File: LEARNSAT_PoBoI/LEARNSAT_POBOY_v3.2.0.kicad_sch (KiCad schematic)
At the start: 0 parts

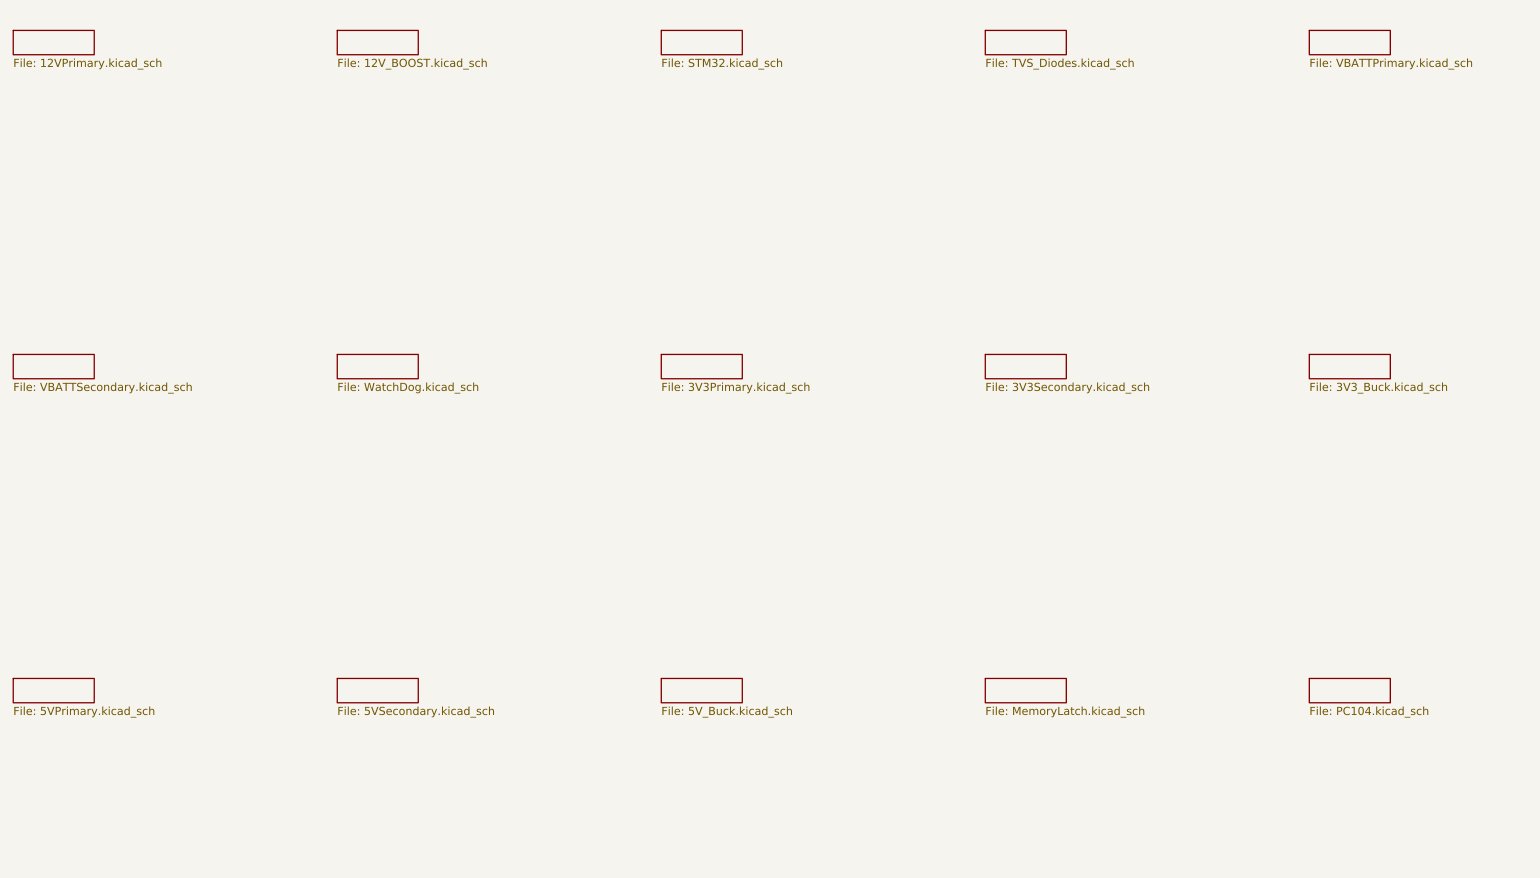
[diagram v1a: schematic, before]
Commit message: Edited 12V Rail schematics
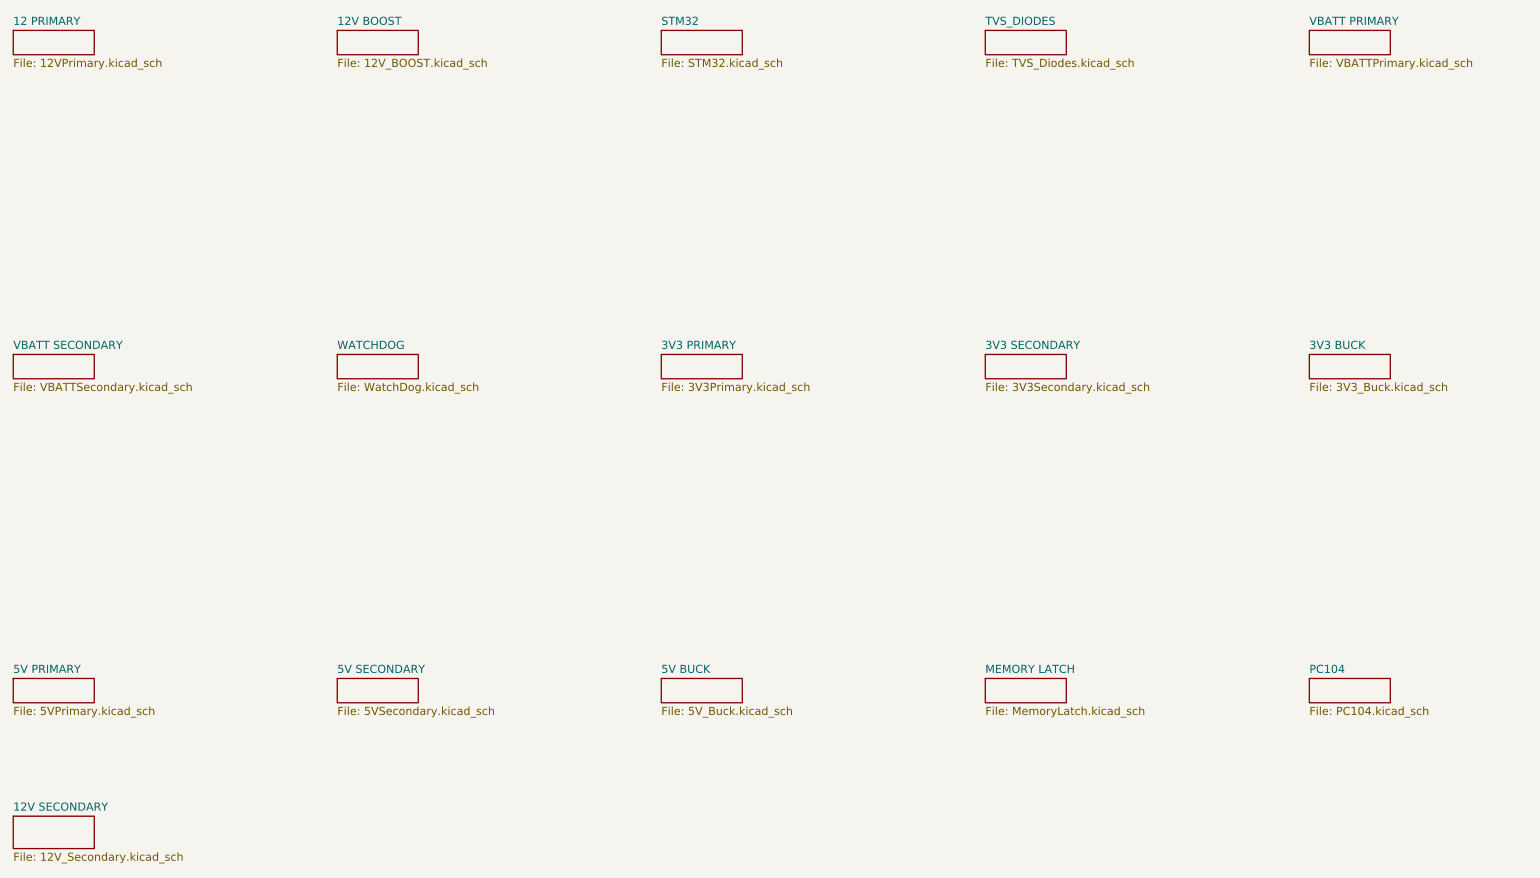
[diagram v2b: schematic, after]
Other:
- sheet  renamed 5V PRIMARY
- added sheet 12 PRIMARY (12VPrimary.kicad_sch)
- added sheet 12V BOOST (12V_BOOST.kicad_sch)
- added sheet 12V SECONDARY (12V_Secondary.kicad_sch)
- added sheet 3V3 BUCK (3V3_Buck.kicad_sch)
- added sheet 3V3 PRIMARY (3V3Primary.kicad_sch)
- added sheet 3V3 SECONDARY (3V3Secondary.kicad_sch)
- added sheet 5V BUCK (5V_Buck.kicad_sch)
- added sheet 5V SECONDARY (5VSecondary.kicad_sch)
- added sheet MEMORY LATCH (MemoryLatch.kicad_sch)
- added sheet PC104 (PC104.kicad_sch)
- added sheet STM32 (STM32.kicad_sch)
- added sheet TVS_DIODES (TVS_Diodes.kicad_sch)
- added sheet VBATT PRIMARY (VBATTPrimary.kicad_sch)
- added sheet VBATT SECONDARY (VBATTSecondary.kicad_sch)
- added sheet WATCHDOG (WatchDog.kicad_sch)
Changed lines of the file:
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@@
 			(color 0 0 0 0)
 		)
-		(property "Sheetname" ""
+		(property "Sheetname" "12V BOOST"
 			(at 76.2 24.6884 0)
 			(show_name no)
@@
 			(color 0 0 0 0)
 		)
-		(property "Sheetname" ""
+		(property "Sheetname" "3V3 BUCK"
 			(at 228.6 75.4884 0)
 			(show_name no)
@@
 			(color 0 0 0 0)
 		)
-		(property "Sheetname" ""
+		(property "Sheetname" "12 PRIMARY"
 			(at 25.4 24.6884 0)
 			(show_name no)
@@
 			(color 0 0 0 0)
 		)
-		(property "Sheetname" ""
+		(property "Sheetname" "WATCHDOG"
 			(at 76.2 75.4884 0)
 			(show_name no)
@@
 			(color 0 0 0 0)
 		)
-		(property "Sheetname" ""
+		(property "Sheetname" "VBATT PRIMARY"
 			(at 228.6 24.6884 0)
 			(show_name no)
@@
 			(color 0 0 0 0)
 		)
-		(property "Sheetname" ""
+		(property "Sheetname" "VBATT SECONDARY"
 			(at 25.4 75.4884 0)
 			(show_name no)
@@
 			(color 0 0 0 0)
 		)
-		(property "Sheetname" ""
+		(property "Sheetname" "5V SECONDARY"
 			(at 76.2 126.2884 0)
 			(show_name no)
@@
 			(color 0 0 0 0)
 		)
-		(property "Sheetname" ""
+		(property "Sheetname" "TVS_DIODES"
 			(at 177.8 24.6884 0)
 			(show_name no)
@@
 			(color 0 0 0 0)
 		)
-		(property "Sheetname" ""
+		(property "Sheetname" "STM32"
 			(at 127 24.6884 0)
 			(show_name no)
@@
 			(color 0 0 0 0)
 		)
-		(property "Sheetname" ""
+		(property "Sheetname" "3V3 SECONDARY"
 			(at 177.8 75.4884 0)
 			(show_name no)
@@
 			(color 0 0 0 0)
 		)
-		(property "Sheetname" ""
+		(property "Sheetname" "MEMORY LATCH"
 			(at 177.8 126.2884 0)
 			(show_name no)
@@
 			(color 0 0 0 0)
 		)
-		(property "Sheetname" ""
+		(property "Sheetname" "3V3 PRIMARY"
 			(at 127 75.4884 0)
 			(show_name no)
@@
 	)
 	(sheet
+		(at 25.4 148.59)
+		(size 12.7 5.08)
+		(exclude_from_sim no)
+		(in_bom yes)
+		(on_board yes)
+		(dnp no)
+		(fields_autoplaced yes)
+		(stroke
+			(width 0.1524)
+			(type solid)
+		)
+		(fill
+			(color 0 0 0 0)
+		)
+		(property "Sheetname" "12V SECONDARY"
+			(at 25.4 147.8784 0)
+			(show_name no)
+			(do_not_autoplace no)
+			(effects
+				(font
+					(size 1.27 1.27)
+				)
+				(justify left bottom)
+			)
+		)
+		(property "Sheetfile" "12V_Secondary.kicad_sch"
+			(at 25.4 154.2546 0)
+			(show_name no)
+			(do_not_autoplace no)
+			(effects
+				(font
+					(size 1.27 1.27)
+				)
+				(justify left top)
+			)
+		)
+		(instances
+			(project "LEARNSAT_POBOY_v3.2.0"
+				(path "/31302da5-a970-4b2b-aa05-afcd06cb9d09"
+					(page "1")
+				)
+			)
+		)
+	)
+	(sheet
 		(at 228.6 127)
 		(size 12.7 3.81)
@@
 			(color 0 0 0 0)
 		)
-		(property "Sheetname" ""
+		(property "Sheetname" "PC104"
 			(at 228.6 126.2884 0)
 			(show_name no)
@@
 			(color 0 0 0 0)
 		)
-		(property "Sheetname" ""
+		(property "Sheetname" "5V BUCK"
 			(at 127 126.2884 0)
 			(show_name no)
@@
 			(color 0 0 0 0)
 		)
-		(property "Sheetname" ""
+		(property "Sheetname" "5V PRIMARY"
 			(at 25.4 126.2884 0)
 			(show_name no)
